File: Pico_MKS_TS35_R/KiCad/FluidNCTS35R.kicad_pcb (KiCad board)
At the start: 2 copper layers, 110 x 65 mm, 13 parts, among them J1 Conn_01x03_Pin, J2 Conn_01x03_Pin, U1 Pico

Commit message: Add PCB
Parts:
- removed G***dfghdfhfgjhtzjftzjtjhrthrheherherherh: LOGO, KiCadFootprintLib:logo_tp_zahnrad_klein
- added C1: C_Polarized, Capacitor_SMD:C_1210_3225Metric_Pad1.33x2.70mm_HandSolder, F.Cu at (177.0, 50.8)
- added C2: C_Polarized, Capacitor_SMD:C_1210_3225Metric_Pad1.33x2.70mm_HandSolder, F.Cu at (137.5, 100.2)
- added C3: C_Polarized, Capacitor_SMD:C_1210_3225Metric_Pad1.33x2.70mm_HandSolder, F.Cu at (168.9, 50.8)
- added G***: LOGO, KiCadFootprintLib:logo_tp_zahnrad_klein, F.Cu at (126.2, 88.5)
- J1: footprint Connector_JST:JST_SH_SM03B-SRSS-TB_1x03-1MP_P1.00mm_Horizontal -> Connector_PinSocket_2.54mm:PinSocket_1x03_P2.54mm_Horizontal
- moved J1 6.19 mm to (185.8, 60.8), turned to 180 degrees
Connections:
- net Net-(D1-K) renamed VDD
- net Net-(J1-Pin_1) renamed SWCLK
- net Net-(J1-Pin_3) renamed SWDIO
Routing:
- net +5V: track 53.3 -> 89.6 mm
- net +3V3: track 76.0 -> 99.1 mm
- net UART_TX: track 89.2 -> 84.7 mm
- net VDD: track 108.3 -> 111.9 mm
- net SWCLK: track 55.8 -> 58.7 mm
- net UART_RX: track 86.0 -> 83.6 mm
- net RESET: track 113.8 -> 116.1 mm
- net BEEPER: track 54.2 -> 56.1 mm
- net SWDIO: track 67.1 -> 68.6 mm
- net LCD_RS: track 46.7 -> 48.0 mm
- net LCD_RESET: track 29.9 -> 30.8 mm
- net LCD_CS: track 43.7 -> 43.1 mm
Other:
- board text added: "+"
- board text added: "FluidNC MKS DLC32 to MKS TS35R Bridge V1.0"
- board text added: "SWCLK"
- board text added: "SWDIO"
- board text removed: "DEBUG"
- board text removed: "FluidNC ESP32 to MKS TS35R Bridge V1.0 TP"

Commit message: Add PCB and some button handlers
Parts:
- added TP1: TestPoint, TestPoint:TestPoint_Pad_D2.0mm, F.Cu at (94.2, 94.5)
- added TP10: TestPoint, TestPoint:TestPoint_Pad_D2.0mm, F.Cu at (147.2, 68.0)
- added TP11: TestPoint, TestPoint:TestPoint_Pad_D2.0mm, F.Cu at (94.5, 61.2)
- added TP12: TestPoint, TestPoint:TestPoint_Pad_D2.0mm, F.Cu at (180.2, 48.2)
- added TP13: TestPoint, TestPoint:TestPoint_Pad_D2.0mm, F.Cu at (133.5, 97.5)
- added TP14: TestPoint, TestPoint:TestPoint_Pad_D2.0mm, F.Cu at (172.2, 48.2)
- added TP15: TestPoint, TestPoint:TestPoint_Pad_D2.0mm, F.Cu at (169.0, 60.2)
- added TP16: TestPoint, TestPoint:TestPoint_Pad_D2.0mm, F.Cu at (174.0, 60.2)
- added TP2: TestPoint, TestPoint:TestPoint_Pad_D2.0mm, F.Cu at (157.0, 68.0)
- added TP3: TestPoint, TestPoint:TestPoint_Pad_D2.0mm, F.Cu at (152.0, 68.0)
- added TP4: TestPoint, TestPoint:TestPoint_Pad_D2.0mm, F.Cu at (123.2, 68.0)
- added TP5: TestPoint, TestPoint:TestPoint_Pad_D2.0mm, F.Cu at (134.0, 68.0)
- added TP6: TestPoint, TestPoint:TestPoint_Pad_D2.0mm, F.Cu at (127.0, 68.0)
- added TP7: TestPoint, TestPoint:TestPoint_Pad_D2.0mm, F.Cu at (130.5, 68.0)
- added TP8: TestPoint, TestPoint:TestPoint_Pad_D2.0mm, F.Cu at (140.8, 68.0)
- added TP9: TestPoint, TestPoint:TestPoint_Pad_D2.0mm, F.Cu at (137.5, 68.0)
- moved G*** 5.22 mm to (124.8, 83.5)
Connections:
- J2 pad 1: Net-(J2-Pin_1) -> RX
- J2 pad 2: Net-(J2-Pin_2) -> GND
- J2 pad 3: GND -> TX
- U1 pad 1: Net-(J2-Pin_1) -> TX
- U1 pad 2: Net-(J2-Pin_2) -> RX
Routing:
- net LCD_RS: track 48.0 -> 99.9 mm
- net +3V3: track 99.1 -> 117.1 mm, vias 0 -> 1
- net Net-(J2-Pin_1): track 17.4 -> 0.00 mm
- net TOUCH_CS: track 45.0 -> 61.8 mm
- net RX: track 0.00 -> 16.3 mm
- net Net-(J2-Pin_2): track 13.8 -> 0.00 mm
- net TX: track 0.00 -> 12.9 mm
- net MOSI: track 25.2 -> 36.7 mm
- net LCD_BACKLIGHT: track 45.0 -> 55.1 mm
- net MISO: track 23.7 -> 33.0 mm
- net BEEPER: track 56.1 -> 63.9 mm
- net SWCLK: track 58.7 -> 52.7 mm
- net RESET: track 116.1 -> 121.7 mm
- net UART_TX: track 84.7 -> 89.2 mm
- net +5V: track 89.6 -> 93.3 mm
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
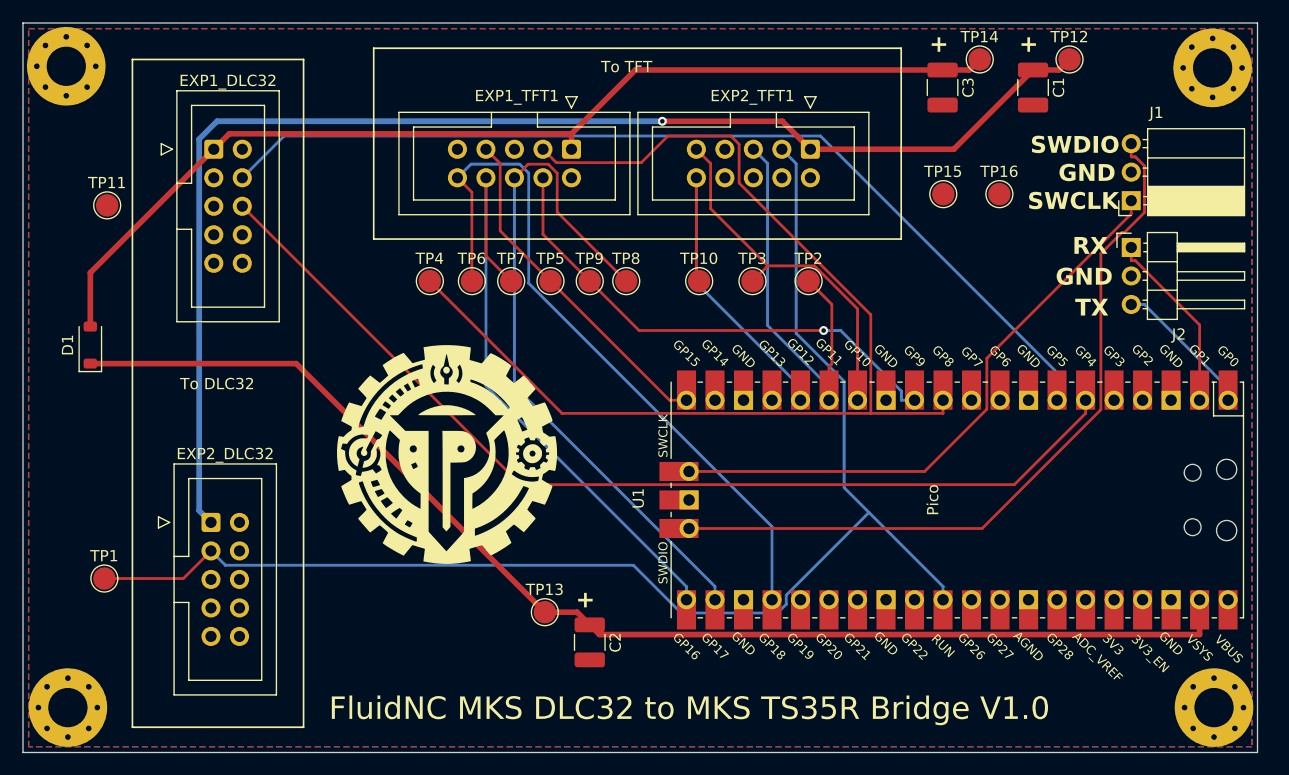
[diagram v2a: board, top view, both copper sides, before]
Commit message: Updated Board. Use GPIO 33 as input
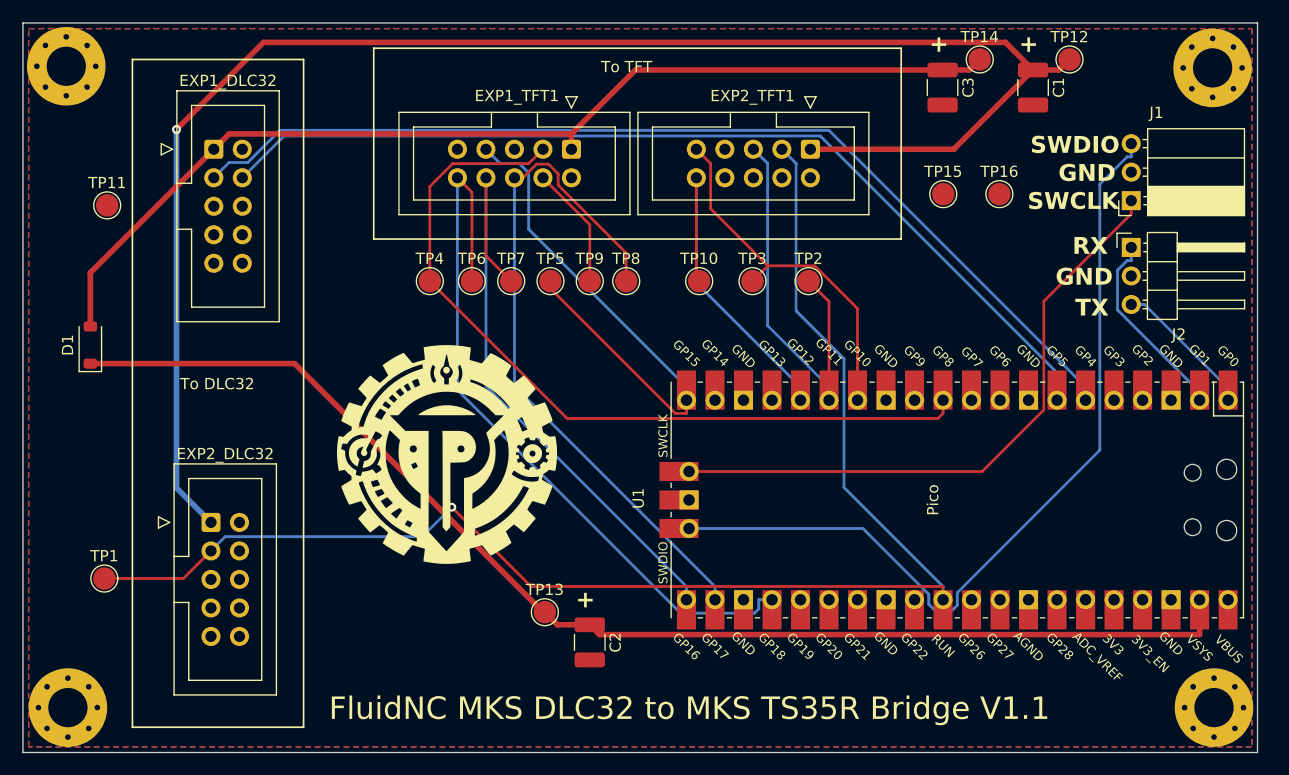
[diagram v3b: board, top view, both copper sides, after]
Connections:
- EXP1_DLC32 pad 3: unconnected-(EXP1_DLC32-Pin_3-Pad3) -> UART_TX
- EXP1_DLC32 pad 6: UART_TX -> unconnected-(EXP1_DLC32-Pin_6-Pad6)
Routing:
- net LCD_CS: track 44.7 -> 10.9 mm, vias 1 -> 0
- net LCD_RS: track 99.9 -> 72.0 mm
- net +3V3: track 117.1 -> 143.2 mm
- net LCD_RESET: track 30.6 -> 49.3 mm
- net SWDIO: track 67.2 -> 75.6 mm
- net RESET: track 121.7 -> 127.6 mm, vias 0 -> 1
- net SWCLK: track 52.7 -> 55.8 mm
- net BEEPER: track 63.9 -> 65.9 mm
- net RX: track 16.3 -> 17.6 mm
- net UART_TX: track 89.2 -> 90.1 mm
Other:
- board text added: "FluidNC MKS DLC32 to MKS TS35R Bridge V1.1"
- board text removed: "FluidNC MKS DLC32 to MKS TS35R Bridge V1.0"
